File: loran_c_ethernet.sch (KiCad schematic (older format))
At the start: 39 parts

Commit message: Almost done: SPI, Relay optocouplers, ADC & DAC interface However, bug needs to be fixed: buses are not connected between hierarchical sheets
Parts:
- C202: renamed from C?; value 2.2u 6.3V -> 2.2u 6.3V Ta
- C204: renamed from C?; value 10n -> 100n
- C207: renamed from C?; value 2.2u 6.3V -> 10u 6.3V Ta
- gave numbers to parts that had none: 36

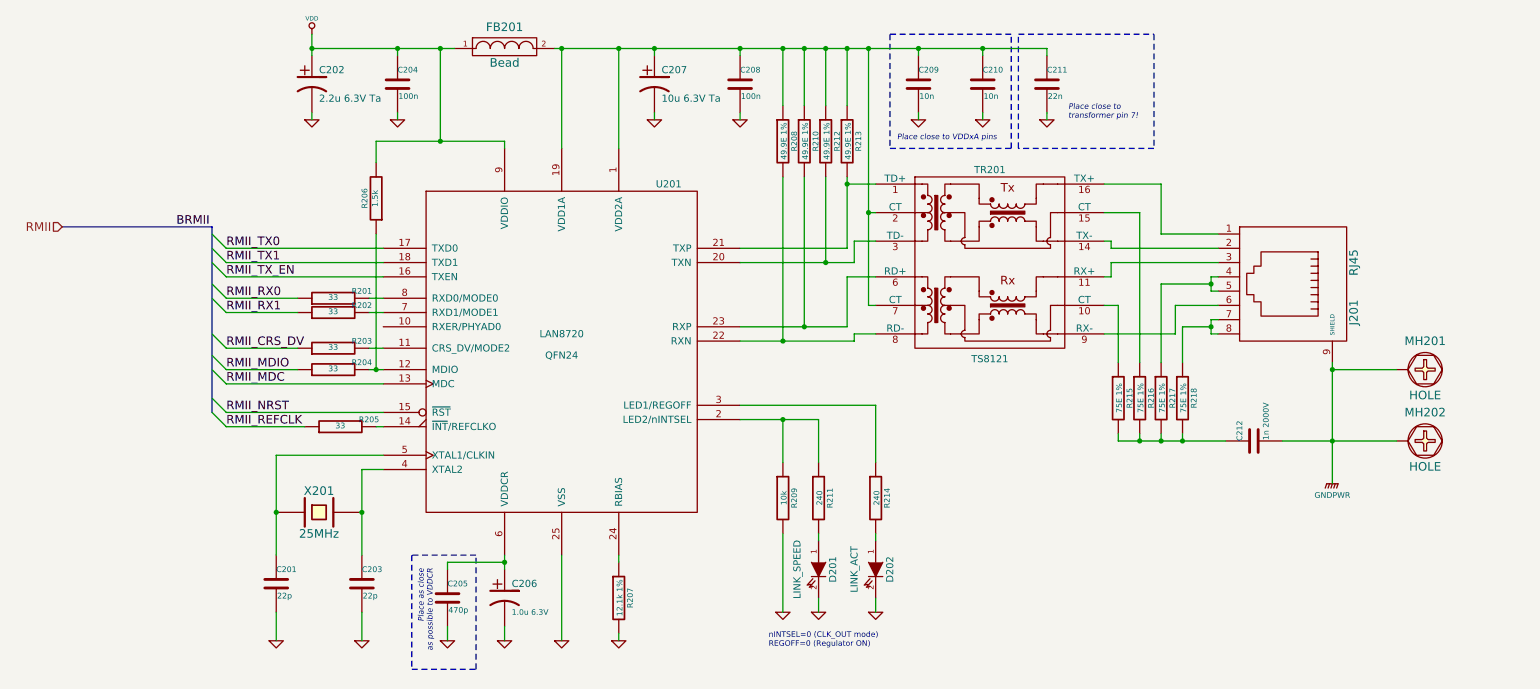
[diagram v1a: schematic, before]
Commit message: FIXED: no more buses on hierarchical sheet ports
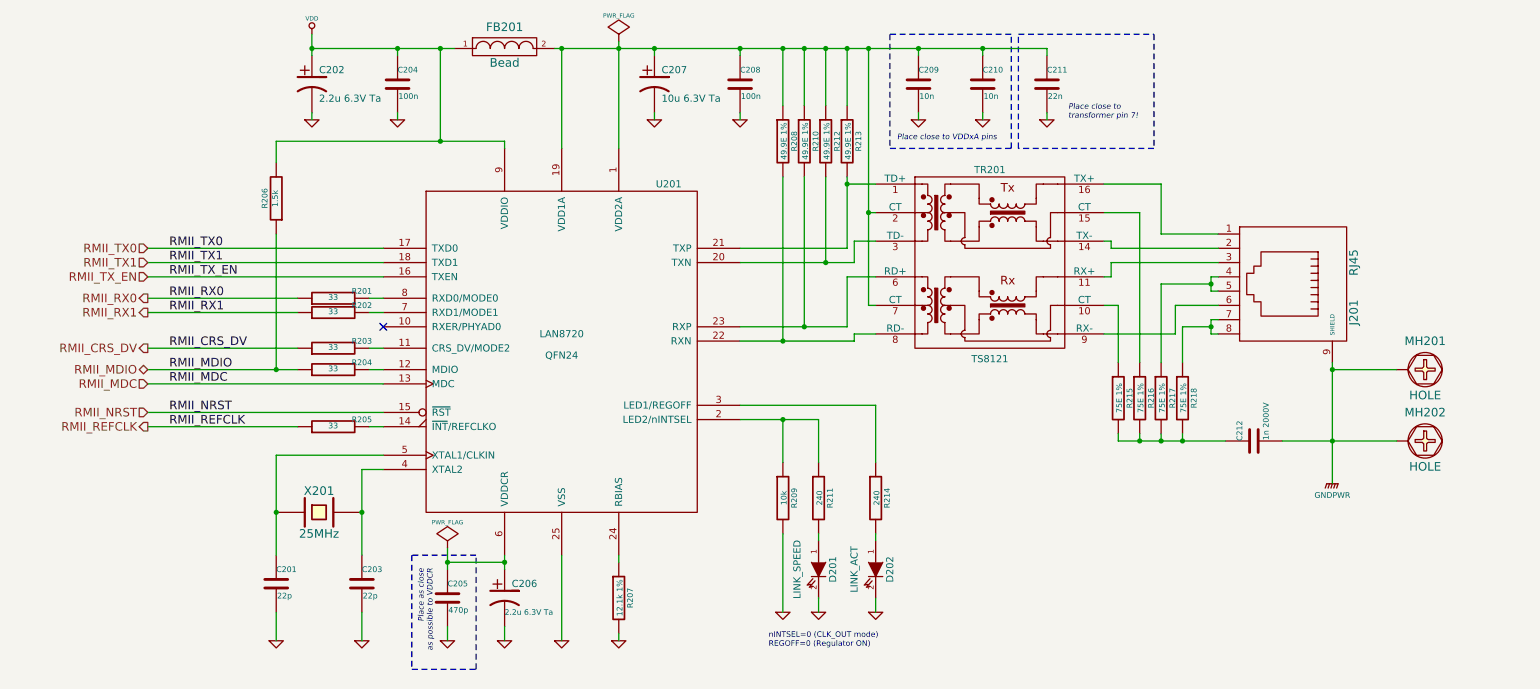
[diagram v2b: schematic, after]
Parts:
- C206: value 1.0u 6.3V -> 2.2u 6.3V Ta
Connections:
- net RMII_MDIO: now also R206.1
- net at R204.2, U201.12 (MDIO): no longer R206.1
- no-connect marks 0 -> 1
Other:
- moved on the sheet: R205, R206
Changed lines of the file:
@@
 $Descr A4 11693 8268
 encoding utf-8
-Sheet 2 7
+Sheet 6 7
 Title "Ethernet PHY"
 Date "18 янв. 2014"
@@
 $EndComp
 $Comp
-L GNDPWR #PWR030
+L GNDPWR #PWR0106
 U 1 1 52D9FC92
 P 9900 4450
-F 0 "#PWR030" H 9900 4500 40  0001 C CNN
+F 0 "#PWR0106" H 9900 4500 40  0001 C CNN
 F 1 "GNDPWR" H 9900 4370 40  0000 C CNN
 F 2 "" H 9900 4450 60  0000 C CNN
@@
 $EndComp
 $Comp
-L GND #PWR031
+L GND #PWR0107
 U 1 1 52DA3B72
 P 4500 5550
-F 0 "#PWR031" H 4500 5550 30  0001 C CNN
+F 0 "#PWR0107" H 4500 5550 30  0001 C CNN
 F 1 "GND" H 4500 5480 30  0001 C CNN
 F 2 "" H 4500 5550 60  0000 C CNN
@@
 $EndComp
 $Comp
-L GND #PWR032
+L GND #PWR0108
 U 1 1 52DA5344
 P 6050 5350
-F 0 "#PWR032" H 6050 5350 30  0001 C CNN
+F 0 "#PWR0108" H 6050 5350 30  0001 C CNN
 F 1 "GND" H 6050 5280 30  0001 C CNN
 F 2 "" H 6050 5350 60  0000 C CNN
@@
 $EndComp
 $Comp
-L GND #PWR033
+L GND #PWR0109
 U 1 1 52DA534F
 P 6300 5350
-F 0 "#PWR033" H 6300 5350 30  0001 C CNN
+F 0 "#PWR0109" H 6300 5350 30  0001 C CNN
 F 1 "GND" H 6300 5280 30  0001 C CNN
 F 2 "" H 6300 5350 60  0000 C CNN
@@
 $EndComp
 $Comp
-L GND #PWR034
+L GND #PWR0110
 U 1 1 52DA6C43
 P 6700 5350
-F 0 "#PWR034" H 6700 5350 30  0001 C CNN
+F 0 "#PWR0110" H 6700 5350 30  0001 C CNN
 F 1 "GND" H 6700 5280 30  0001 C CNN
 F 2 "" H 6700 5350 60  0000 C CNN
@@
 P 4100 5250
 F 0 "C206" H 4150 5350 50  0000 L CNN
-F 1 "1.0u 6.3V" H 4150 5150 39  0000 L CNN
+F 1 "2.2u 6.3V Ta" H 4100 5150 39  0000 L CNN
 F 2 "" H 4100 5250 60  0000 C CNN
 F 3 "" H 4100 5250 60  0000 C CNN
@@
 $EndComp
 $Comp
-L GND #PWR035
+L GND #PWR0111
 U 1 1 52DA7E33
 P 4100 5550
-F 0 "#PWR035" H 4100 5550 30  0001 C CNN
+F 0 "#PWR0111" H 4100 5550 30  0001 C CNN
 F 1 "GND" H 4100 5480 30  0001 C CNN
 F 2 "" H 4100 5550 60  0000 C CNN
@@
 nINTSEL=0 (CLK_OUT mode)\nREGOFF=0 (Regulator ON)
 $Comp
-L GND #PWR036
+L GND #PWR0112
 U 1 1 52DA9EA3
 P 4900 5550
-F 0 "#PWR036" H 4900 5550 30  0001 C CNN
+F 0 "#PWR0112" H 4900 5550 30  0001 C CNN
 F 1 "GND" H 4900 5480 30  0001 C CNN
 F 2 "" H 4900 5550 60  0000 C CNN
@@
 $EndComp
 $Comp
-L GND #PWR037
+L GND #PWR0113
 U 1 1 52DAE216
 P 7450 1900
-F 0 "#PWR037" H 7450 1900 30  0001 C CNN
+F 0 "#PWR0113" H 7450 1900 30  0001 C CNN
 F 1 "GND" H 7450 1830 30  0001 C CNN
 F 2 "" H 7450 1900 60  0000 C CNN
@@
 	7450 1850 7450 1900
 $Comp
-L GND #PWR038
+L GND #PWR0114
 U 1 1 52DAE39A
 P 7000 1900
-F 0 "#PWR038" H 7000 1900 30  0001 C CNN
+F 0 "#PWR0114" H 7000 1900 30  0001 C CNN
 F 1 "GND" H 7000 1830 30  0001 C CNN
 F 2 "" H 7000 1900 60  0000 C CNN
@@
 $EndComp
 $Comp
-L GND #PWR039
+L GND #PWR0115
 U 1 1 52DAE3A5
 P 5150 1900
-F 0 "#PWR039" H 5150 1900 30  0001 C CNN
+F 0 "#PWR0115" H 5150 1900 30  0001 C CNN
 F 1 "GND" H 5150 1830 30  0001 C CNN
 F 2 "" H 5150 1900 60  0000 C CNN
@@
 Connection ~ 6050 1400
 Wire Wire Line
-	4900 1400 4900 2100
+	4900 1350 4900 2100
 Connection ~ 4900 1400
 Wire Wire Line
@@
 Connection ~ 2500 4650
 $Comp
-L GND #PWR040
+L GND #PWR0116
 U 1 1 52DB2EE5
 P 3100 5550
-F 0 "#PWR040" H 3100 5550 30  0001 C CNN
+F 0 "#PWR0116" H 3100 5550 30  0001 C CNN
 F 1 "GND" H 3100 5480 30  0001 C CNN
 F 2 "" H 3100 5550 60  0000 C CNN
@@
 $EndComp
 $Comp
-L GND #PWR041
+L GND #PWR0117
 U 1 1 52DB2EF0
 P 2500 5550
-F 0 "#PWR041" H 2500 5550 30  0001 C CNN
+F 0 "#PWR0117" H 2500 5550 30  0001 C CNN
 F 1 "GND" H 2500 5480 30  0001 C CNN
 F 2 "" H 2500 5550 60  0000 C CNN
@@
 $EndComp
 $Comp
-L GND #PWR042
+L GND #PWR0118
 U 1 1 52DB3FBE
 P 7900 1900
-F 0 "#PWR042" H 7900 1900 30  0001 C CNN
+F 0 "#PWR0118" H 7900 1900 30  0001 C CNN
 F 1 "GND" H 7900 1830 30  0001 C CNN
 F 2 "" H 7900 1900 60  0000 C CNN
@@
 $EndComp
 $Comp
-L GND #PWR043
+L GND #PWR0119
 U 1 1 52D9C546
 P 3700 5550
-F 0 "#PWR043" H 3700 5550 30  0001 C CNN
+F 0 "#PWR0119" H 3700 5550 30  0001 C CNN
 F 1 "GND" H 3700 5480 30  0001 C CNN
 F 2 "" H 3700 5550 60  0000 C CNN
@@
 	3700 5450 3700 5550
 Wire Wire Line
-	3700 5050 3700 5000
+	3700 4900 3700 5050
 Wire Wire Line
 	3700 5000 4100 5000
@@
 L R R205
 U 1 1 52D9DCAC
-P 2950 4050
-F 0 "R205" V 3000 3850 40  0000 C CNN
-F 1 "33" V 2957 4051 40  0000 C CNN
-F 2 "" V 2880 4050 30  0000 C CNN
-F 3 "" H 2950 4050 30  0000 C CNN
-	1    2950 4050
+P 2900 4050
+F 0 "R205" V 2950 3850 40  0000 C CNN
+F 1 "33" V 2907 4051 40  0000 C CNN
+F 2 "" V 2830 4050 30  0000 C CNN
+F 3 "" H 2900 4050 30  0000 C CNN
+	1    2900 4050
 	0    -1   -1   0
 $EndComp
 Wire Wire Line
-	3250 4050 3200 4050
+	3250 4050 3150 4050
 Text Notes 6850 2050 0    39   Italic 0
 Place close to VDDxA pins
@@
 $EndComp
 $Comp
-L GND #PWR044
+L GND #PWR0120
 U 1 1 52DA14D5
 P 5750 1900
-F 0 "#PWR044" H 5750 1900 30  0001 C CNN
+F 0 "#PWR0120" H 5750 1900 30  0001 C CNN
 F 1 "GND" H 5750 1830 30  0001 C CNN
 F 2 "" H 5750 1900 60  0000 C CNN
@@
 	4100 2050 4100 2100
 Wire Wire Line
-	3200 2050 4100 2050
+	2500 2050 4100 2050
 Wire Wire Line
 	3650 1400 3650 2050
@@
 Connection ~ 3350 1400
 $Comp
-L GND #PWR045
+L GND #PWR0121
 U 1 1 52DA3A63
 P 2750 1900
-F 0 "#PWR045" H 2750 1900 30  0001 C CNN
+F 0 "#PWR0121" H 2750 1900 30  0001 C CNN
 F 1 "GND" H 2750 1830 30  0001 C CNN
 F 2 "" H 2750 1900 60  0000 C CNN
@@
 $EndComp
 $Comp
-L GND #PWR046
+L GND #PWR0122
 U 1 1 52DA3A6E
 P 3350 1900
-F 0 "#PWR046" H 3350 1900 30  0001 C CNN
+F 0 "#PWR0122" H 3350 1900 30  0001 C CNN
 F 1 "GND" H 3350 1830 30  0001 C CNN
 F 2 "" H 3350 1900 60  0000 C CNN
@@
 	2750 1850 2750 1900
 $Comp
-L VDD #PWR047
+L VDD #PWR0123
 U 1 1 52DA4656
 P 2750 1300
-F 0 "#PWR047" H 2750 1400 30  0001 C CNN
+F 0 "#PWR0123" H 2750 1400 30  0001 C CNN
 F 1 "VDD" H 2750 1410 30  0000 C CNN
 F 2 "" H 2750 1300 60  0000 C CNN
@@
 L R R206
 U 1 1 52DA533B
-P 3200 2450
-F 0 "R206" V 3280 2450 40  0000 C CNN
-F 1 "1.5k" V 3207 2451 40  0000 C CNN
-F 2 "" V 3130 2450 30  0000 C CNN
-F 3 "" H 3200 2450 30  0000 C CNN
-	1    3200 2450
+P 2500 2450
+F 0 "R206" V 2580 2450 40  0000 C CNN
+F 1 "1.5k" V 2507 2451 40  0000 C CNN
+F 2 "" V 2430 2450 30  0000 C CNN
+F 3 "" H 2500 2450 30  0000 C CNN
+	1    2500 2450
 	-1   0    0    1
 $EndComp
-Wire Wire Line
-	3200 2700 3200 3650
 Wire Wire Line
 	3150 3650 3250 3650
 Connection ~ 3650 2050
-Wire Wire Line
-	3200 2200 3200 2050
 $Comp
 L R R201
@@
 	0    -1   -1   0
 $EndComp
-Connection ~ 3200 3650
-Wire Bus Line
-	2050 2650 2050 3950
-Wire Wire Line
-	3250 2800 2150 2800
-Wire Wire Line
-	3250 2900 2150 2900
-Wire Wire Line
-	3250 3000 2150 3000
-Wire Wire Line
-	2650 3150 2150 3150
-Wire Wire Line
-	2650 3250 2150 3250
-Wire Wire Line
-	2650 3500 2150 3500
-Wire Wire Line
-	2650 3650 2150 3650
-Wire Wire Line
-	2700 4050 2150 4050
-Entry Wire Line
-	2050 3950 2150 4050
-Entry Wire Line
-	2050 3550 2150 3650
-Entry Wire Line
-	2050 3400 2150 3500
-Entry Wire Line
-	2050 3150 2150 3250
-Entry Wire Line
-	2050 3050 2150 3150
-Entry Wire Line
-	2050 2900 2150 3000
-Entry Wire Line
-	2050 2800 2150 2900
-Entry Wire Line
-	2050 2700 2150 2800
-Wire Wire Line
-	3250 3950 2150 3950
-Entry Wire Line
-	2050 3850 2150 3950
-Text Label 2150 3950 0    60   ~ 0
+Wire Wire Line
+	1600 2800 3250 2800
+Wire Wire Line
+	1600 2900 3250 2900
+Wire Wire Line
+	1600 3000 3250 3000
+Wire Wire Line
+	1600 3150 2650 3150
+Wire Wire Line
+	1600 3250 2650 3250
+Wire Wire Line
+	1600 3500 2650 3500
+Wire Wire Line
+	1600 3650 2650 3650
+Wire Wire Line
+	1600 4050 2650 4050
+Wire Wire Line
+	1600 3950 3250 3950
+Text Label 1750 3950 0    60   ~ 0
 RMII_NRST
-Text Label 2150 4050 0    60   ~ 0
+Text Label 1750 4050 0    60   ~ 0
 RMII_REFCLK
-Text Label 2150 3650 0    60   ~ 0
+Text Label 1750 3650 0    60   ~ 0
 RMII_MDIO
 Wire Wire Line
-	3250 3750 2150 3750
-Entry Wire Line
-	2050 3650 2150 3750
-Text Label 2150 3750 0    60   ~ 0
+	1600 3750 3250 3750
+Text Label 1750 3750 0    60   ~ 0
 RMII_MDC
-Text Label 2150 3500 0    60   ~ 0
+Text Label 1750 3500 0    60   ~ 0
 RMII_CRS_DV
-Text Label 2150 3250 0    60   ~ 0
+Text Label 1750 3250 0    60   ~ 0
 RMII_RX1
-Text Label 2150 3150 0    60   ~ 0
+Text Label 1750 3150 0    60   ~ 0
 RMII_RX0
-Text Label 2150 3000 0    60   ~ 0
+Text Label 1750 3000 0    60   ~ 0
 RMII_TX_EN
-Text Label 2150 2800 0    60   ~ 0
+Text Label 1750 2800 0    60   ~ 0
 RMII_TX0
-Text Label 2150 2900 0    60   ~ 0
+Text Label 1750 2900 0    60   ~ 0
 RMII_TX1
-Wire Bus Line
-	1000 2650 2050 2650
-Text Label 1800 2650 0    60   ~ 0
-BRMII
 Wire Wire Line
 	5750 1400 5750 1450
@@
 	5150 1400 5150 1450
 Connection ~ 5150 1400
-Text HLabel 1000 2650 0    61   Input ~ 0
-RMII
 Wire Notes Line
 	3450 4950 3450 5750
@@
 Wire Notes Line
 	3900 4950 3450 4950
+Text HLabel 1600 2800 0    60   Input ~ 0
+RMII_TX0
+Text HLabel 1600 2900 0    60   Input ~ 0
+RMII_TX1
+Text HLabel 1600 3000 0    60   Input ~ 0
+RMII_TX_EN
+Text HLabel 1600 3150 0    60   Output ~ 0
+RMII_RX0
+Text HLabel 1600 3250 0    60   Output ~ 0
+RMII_RX1
+Text HLabel 1600 3500 0    60   Output ~ 0
+RMII_CRS_DV
+Text HLabel 1600 3650 0    60   BiDi ~ 0
+RMII_MDIO
+Text HLabel 1600 3750 0    60   Input ~ 0
+RMII_MDC
+Text HLabel 1600 3950 0    60   Input ~ 0
+RMII_NRST
+Text HLabel 1600 4050 0    60   Output ~ 0
+RMII_REFCLK
+Wire Wire Line
+	2500 2700 2500 3650
+Connection ~ 2500 3650
+Wire Wire Line
+	2500 2050 2500 2200
+NoConn ~ 3250 3350
+$Comp
+L PWR_FLAG #FLG0124
+U 1 1 52E8618A
+P 3700 4900
+F 0 "#FLG0124" H 3700 4995 30  0001 C CNN
+F 1 "PWR_FLAG" H 3700 5080 30  0000 C CNN
+F 2 "" H 3700 4900 60  0000 C CNN
+F 3 "" H 3700 4900 60  0000 C CNN
+	1    3700 4900
+	1    0    0    -1
+$EndComp
+Connection ~ 3700 5000
+$Comp
+L PWR_FLAG #FLG0125
+U 1 1 52E86593
+P 4900 1350
+F 0 "#FLG0125" H 4900 1445 30  0001 C CNN
+F 1 "PWR_FLAG" H 4900 1530 30  0000 C CNN
+F 2 "" H 4900 1350 60  0000 C CNN
+F 3 "" H 4900 1350 60  0000 C CNN
+	1    4900 1350
+	1    0    0    -1
+$EndComp
 $EndSCHEMATC
